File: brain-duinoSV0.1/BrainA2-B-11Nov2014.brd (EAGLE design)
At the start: 100.1 x 80 mm, 40 parts, among them IC2 OP2177ARMZ, IC7 LT1761ES5-5

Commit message: BrainA2-B: Getting rid of some schematic level ERC errors and warnings
Signed-off-by: Christoph Maier <cm.hardware.software.elsewhere@gmail.com>
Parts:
- JP5, JP6: value (none) -> .
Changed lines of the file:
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@@
 <attribute name="VALUE" x="44.94" y="39.365" size="0.4064" layer="27" rot="R90"/>
 </element>
-<element name="JP5" library="pinhead" package="1X12" value="" x="52.1" y="46.5" smashed="yes">
+<element name="JP5" library="pinhead" package="1X12" value="." x="52.1" y="46.5" smashed="yes">
 <attribute name="NAME" x="36.0838" y="47.6288" size="0.4064" layer="25" ratio="10"/>
 <attribute name="VALUE" x="36.86" y="43.325" size="1.27" layer="27"/>
 </element>
-<element name="JP6" library="pinhead" package="1X12" value="" x="52.1" y="28.7" smashed="yes">
+<element name="JP6" library="pinhead" package="1X12" value="." x="52.1" y="28.7" smashed="yes">
 <attribute name="NAME" x="36.0838" y="27.2288" size="0.4064" layer="25" ratio="10"/>
 <attribute name="VALUE" x="36.86" y="25.525" size="1.27" layer="27"/>

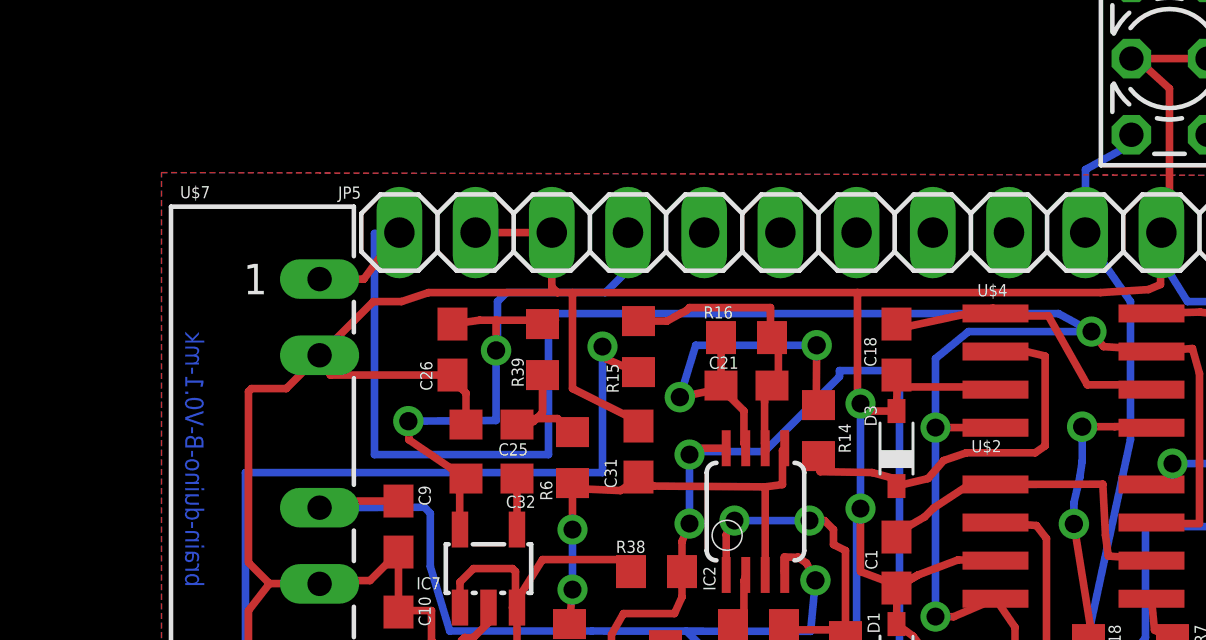
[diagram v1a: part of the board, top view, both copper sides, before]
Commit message: Rename U$2->IC10 U$4->IC11 U$7->IC12
Signed-off-by: Christoph Maier <cm.hardware.software.elsewhere@gmail.com>
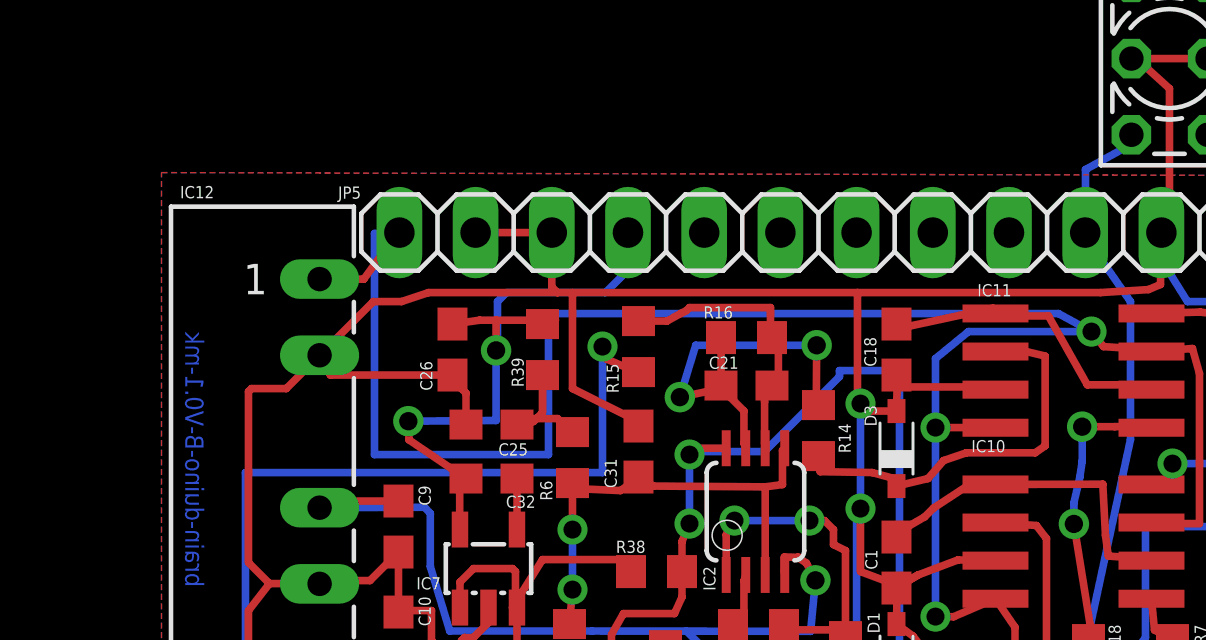
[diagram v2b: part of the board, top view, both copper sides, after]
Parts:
- renumbered U$2 to IC10, U$4 to IC11, U$7 to IC12
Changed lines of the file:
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@@
 <attribute name="VALUE" x="66.73" y="38.86" size="0.4064" layer="27"/>
 </element>
-<element name="U$4" library="MKH" package="MAX7480" value="MAX7480ESA+" x="60.6" y="41.9" smashed="yes" rot="R270">
+<element name="IC11" library="MKH" package="MAX7480" value="MAX7480ESA+" x="60.6" y="41.9" smashed="yes" rot="R270">
 <attribute name="NAME" x="57.395" y="44.375" size="0.4064" layer="25"/>
 <attribute name="VALUE" x="59.495" y="41.755" size="0.4064" layer="27"/>
@@
 <attribute name="VALUE" x="37.06" y="32.97" size="0.4064" layer="27" rot="R270"/>
 </element>
-<element name="U$7" library="MKH" package="RB-0515D" value="DC-DC +-12V, RB-0512D" x="34.2" y="38.6" smashed="yes">
+<element name="IC12" library="MKH" package="RB-0515D" value="DC-DC +-12V, RB-0512D" x="34.2" y="38.6" smashed="yes">
 <attribute name="NAME" x="30.817" y="47.644" size="0.4064" layer="25" ratio="10"/>
 <attribute name="VALUE" x="32.43" y="33.563" size="0.4064" layer="27" ratio="10" rot="R90"/>
@@
 <attribute name="VALUE" x="66.765" y="40.795" size="0.4064" layer="27"/>
 </element>
-<element name="U$2" library="MKH" package="MAX7480" value="MAX7480ESA+" x="60.6" y="36.2" smashed="yes" rot="R270">
+<element name="IC10" library="MKH" package="MAX7480" value="MAX7480ESA+" x="60.6" y="36.2" smashed="yes" rot="R270">
 <attribute name="NAME" x="57.195" y="39.175" size="0.4064" layer="25"/>
 <attribute name="VALUE" x="59.395" y="35.955" size="0.4064" layer="27"/>
@@
 <signals>
 <signal name="GND">
-<contactref element="U$4" pad="3"/>
+<contactref element="IC11" pad="3"/>
 <contactref element="C19" pad="1"/>
 <contactref element="C18" pad="1"/>
@@
 <contactref element="R29" pad="1"/>
 <contactref element="C15" pad="1"/>
-<contactref element="U$7" pad="2"/>
+<contactref element="IC12" pad="2"/>
 <contactref element="C20" pad="1"/>
-<contactref element="U$2" pad="3"/>
+<contactref element="IC10" pad="3"/>
 <contactref element="C16" pad="1"/>
 <contactref element="C1" pad="1"/>
@@
 <contactref element="C23" pad="1"/>
 <contactref element="C24" pad="1"/>
-<contactref element="U$7" pad="5"/>
+<contactref element="IC12" pad="5"/>
 <contactref element="C10" pad="1"/>
 <contactref element="C9" pad="2"/>
@@
 <contactref element="C10" pad="2"/>
 <contactref element="R38" pad="1"/>
-<contactref element="U$7" pad="6"/>
+<contactref element="IC12" pad="6"/>
 <wire x1="35.52" y1="32.2" x2="35.47" y2="32.25" width="0.254" layer="1"/>
 <wire x1="38.1" y1="32.15" x2="35.57" y2="32.15" width="0.254" layer="1"/>
@@
 </signal>
 <signal name="V-">
-<contactref element="U$7" pad="4"/>
+<contactref element="IC12" pad="4"/>
 <contactref element="IC2" pad="4"/>
 <contactref element="C9" pad="1"/>
@@
 <signal name="N$39">
 <contactref element="C18" pad="2"/>
-<contactref element="U$4" pad="6"/>
-<contactref element="U$4" pad="1"/>
+<contactref element="IC11" pad="6"/>
+<contactref element="IC11" pad="1"/>
 <wire x1="57.918" y1="43.9795" x2="55.123" y2="43.3795" width="0.254" layer="1"/>
 <wire x1="57.9475" y1="43.95" x2="57.918" y2="43.9795" width="0.254" layer="1"/>
@@
 <signal name="N$46">
 <contactref element="R18" pad="1"/>
-<contactref element="U$4" pad="5"/>
+<contactref element="IC11" pad="5"/>
 <wire x1="61.154" y1="33.429" x2="61.054" y2="32.8045" width="0.254" layer="1"/>
 <wire x1="60.613" y1="36.788" x2="61.154" y2="33.429" width="0.254" layer="1"/>
@@
 </signal>
 <signal name="N$11">
-<contactref element="U$4" pad="2"/>
+<contactref element="IC11" pad="2"/>
 <contactref element="D3" pad="C"/>
 <contactref element="R14" pad="2"/>
@@
 </signal>
 <signal name="VCC">
-<contactref element="U$4" pad="4"/>
-<contactref element="U$4" pad="7"/>
-<contactref element="U$2" pad="4"/>
-<contactref element="U$2" pad="7"/>
-<contactref element="U$7" pad="1"/>
+<contactref element="IC11" pad="4"/>
+<contactref element="IC11" pad="7"/>
+<contactref element="IC10" pad="4"/>
+<contactref element="IC10" pad="7"/>
+<contactref element="IC12" pad="1"/>
 <contactref element="C20" pad="2"/>
 <contactref element="JP5" pad="1"/>
@@
 </signal>
 <signal name="N$91">
-<contactref element="U$4" pad="8"/>
+<contactref element="IC11" pad="8"/>
 <contactref element="C23" pad="2"/>
 <contactref element="C27" pad="2"/>
@@
 <signal name="N$6">
 <contactref element="C1" pad="2"/>
-<contactref element="U$2" pad="6"/>
-<contactref element="U$2" pad="1"/>
+<contactref element="IC10" pad="6"/>
+<contactref element="IC10" pad="1"/>
 <wire x1="55.641" y1="37.024" x2="55.123" y2="36.724" width="0.254" layer="1"/>
 <wire x1="55.9295" y1="37.3125" x2="55.641" y2="37.024" width="0.254" layer="1"/>
@@
 <signal name="N$13">
 <contactref element="R7" pad="1"/>
-<contactref element="U$2" pad="5"/>
+<contactref element="IC10" pad="5"/>
 <wire x1="63.2" y1="34.295" x2="63.3" y2="33.25" width="0.254" layer="1"/>
 <wire x1="63.3" y1="33.25" x2="63.9" y2="32.95" width="0.254" layer="1"/>
 </signal>
 <signal name="N$14">
-<contactref element="U$2" pad="2"/>
+<contactref element="IC10" pad="2"/>
 <contactref element="D1" pad="C"/>
 <contactref element="R11" pad="2"/>
@@
 </signal>
 <signal name="N$15">
-<contactref element="U$2" pad="8"/>
+<contactref element="IC10" pad="8"/>
 <contactref element="C24" pad="2"/>
 <contactref element="C28" pad="2"/>
